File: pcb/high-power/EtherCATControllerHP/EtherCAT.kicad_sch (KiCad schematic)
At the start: 45 parts, among them U7 LAN9252I/ML, U9 24FC512-I/SN, Y2 25 MHz, 20ppm

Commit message: starting HP version
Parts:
- removed C11, C33, C35, C62: 0.1uF, symbol Device:C_Small
- removed C30, C31: 18pF, symbol Device:C_Small
- removed C32, C34: 1uF, symbol Device:C_Small
- removed C71, C72: 10pF, symbol Device:C_Small
- removed R10, R19, R34: 49.9, symbol Device:R_Small
- removed R22: 0, symbol Device:R_Small
- removed R25: 4.7k, symbol Device:R_Small
- removed R26, R43: 2k, symbol Device:R_Small
- removed R7: 12.1K, symbol Device:R_Small
- removed U7: LAN9252I/ML, QFN64_ML_MCH, symbol 2024-07-01_21-03-15:LAN9252I_ML
- removed U9: 24FC512-I/SN, SOIC8_4P9X3P9MC_MCH, symbol 2024-07-03_18-39-37:24FC512-I_SN
- added C38, C39: 18pF, Capacitor_SMD:C_0402_1005Metric, symbol Device:C_Small
- added C50, C53, C55, C57, C75: 0.1uF, Capacitor_SMD:C_0603_1608Metric, symbol Device:C_Small
- added C51, C52: 1uF, Capacitor_SMD:C_0603_1608Metric, symbol Device:C_Small
- added C54: 470pF, Capacitor_SMD:C_0402_1005Metric, symbol Device:C_Small
- added RN1, RN2: 49R9, Resistor_SMD:R_Array_Convex_4x0402, symbol Device:R_Pack04_Split
- added U4: LAN9252I/ML, footprints:QFN64_ML_MCH, symbol 2024-07-01_21-03-15:LAN9252I_ML
- added U7: 24FC512-I/SN, Package_SO:SOP-8_3.9x4.9mm_P1.27mm, symbol 2024-07-03_18-39-37:24FC512-I_SN
- C36: value 0.1uF -> 1uF; footprint (none) -> Capacitor_SMD:C_0603_1608Metric; LCSC Part # (none) -> C106858
- C58: value 1uF -> 0.1uF; footprint (none) -> Capacitor_SMD:C_0603_1608Metric; LCSC Part # (none) -> C77055
- C59, C61, C63: value 0.1uF -> 10pF; footprint (none) -> Capacitor_SMD:C_0402_1005Metric; LCSC Part # (none) -> C115606
- C60: value 470pF -> 10pF; footprint (none) -> Capacitor_SMD:C_0402_1005Metric; LCSC Part # (none) -> C115606
- C64, C65, C66, C67: footprint (none) -> Capacitor_SMD:C_0402_1005Metric; LCSC Part # (none) -> C115606
- C68: footprint (none) -> Capacitor_SMD:C_0402_1005Metric; LCSC Part # (none) -> C147616
- C69: value 10pF -> 0.022uF; footprint (none) -> Capacitor_SMD:C_0402_1005Metric; LCSC Part # (none) -> C147616
- C70: value 10pF -> 0.1uF; footprint (none) -> Capacitor_SMD:C_0603_1608Metric; LCSC Part # (none) -> C77055
- C73: value 0.022uF -> 0.1uF; footprint (none) -> Capacitor_SMD:C_0603_1608Metric; LCSC Part # (none) -> C77055
- FB1, FB2, FB3, FB4: footprint (none) -> Inductor_SMD:L_1206_3216Metric; LCSC Part # (none) -> C380287
- R33, R9: value 49.9 -> 0; footprint (none) -> Resistor_SMD:R_0402_1005Metric; LCSC Part # (none) -> C106231
- R35: value 49.9 -> 4.7k; footprint (none) -> Resistor_SMD:R_0402_1005Metric; LCSC Part # (none) -> C105871
- R36: value 49.9 -> 12.1K; footprint (none) -> Resistor_SMD:R_0402_1005Metric; LCSC Part # (none) -> C281773
- R37: value 0 -> 2k; footprint (none) -> Resistor_SMD:R_0402_1005Metric; LCSC Part # (none) -> C144035
- R8: value 49.9 -> 2k; footprint (none) -> Resistor_SMD:R_0402_1005Metric; LCSC Part # (none) -> C144035
- Y2: value 25 MHz, 20ppm -> ABM8-25.000MHZ-D2Y-T; footprint (none) -> Crystal:Crystal_SMD_3225-4Pin_3.2x2.5mm; LCSC Part # (none) -> C179643; LCSC Part Number C179643 -> (none)
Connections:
- net ETH0_CT1: now also R33.2
- net ETH0_RXN: now also C61.1, RN1.2 (R2.1), U4.61 (RXNB); no longer C65.1, R9.2
- net ETH0_RXP: now also C59.1, RN1.1 (R1.1), U4.60 (RXPB); no longer C64.1, R8.2
- net ETH0_TXN: now also C66.1, RN1.4 (R4.1), U4.63 (TXNB); no longer C67.1
- net ETH0_TXP: now also C64.1, RN1.3 (R3.1), U4.62 (TXPB); no longer C66.1
- net ETH1_CT1: now also C69.1, R9.2; no longer C73.1, R37.2
- net ETH1_RXN: now also C65.1, RN2.3 (R3.1), U4.54 (RXNA); no longer R35.2
- net ETH1_RXP: now also C67.1, RN2.4 (R4.1), U4.55 (RXPA); no longer R36.2
- net ETH1_TXN: now also C60.1, RN2.1 (R1.1), U4.52 (TXNA); no longer C69.1, R33.2
- net ETH1_TXP: now also C63.1, RN2.2 (R2.1), U4.53 (TXPA); no longer C70.1
- net EtherCAT3v3: now also R37.1, R8.1, C75.1, U4.14 (VDDIO), U4.20 (VDDIO), U4.32 (VDDIO), U4.37 (VDDIO), U4.47 (VDDIO), U4.5 (VDD33), U4.7 (REG_EN), U7.8 (VCC)
- net GND: now also R35.2, R36.2, C38.1, C39.1, C50.2, C51.2, C52.2, C53.2, C54.2, C55.2, C57.2, C75.2, U4.10 (FXSDB/FXLOSB/FXSDENB), U4.4 (OSCVSS), U4.41 (TESTMODE), U4.65 (VSS), U4.8 (FXLOSEN), U4.9 (FXSDA/FXLOSA/FXSDENA), U7.4 (VSS)
- net I2C_SCL: now also R37.2, U4.43 (EESCL/TCK), U7.6 (SCL)
- net IRQ: now also U4.44 (IRQ)
- net RST: now also U4.11 (RST#)
- net SPI_CS: now also U4.50 (D5/AD5/OUTVALID/SCS#)
- net SPI_MISO: now also U4.13 (D1/AD1/EOF/SO/SIO1)
- net SPI_MOSI: now also U4.17 (D0/AD0/WD_STATE/SI/SIO0)
- net SPI_SCK: now also U4.19 (D9/AD9/LATCH_IN/SCK)
- net VDDBIAS: now also C53.1, U4.58 (VDD33BIAS); no longer C36.1
- net VDDCR: now also C36.1, C50.1, C54.1, U4.24 (VDDCR), U4.38 (VDDCR), U4.6 (VDDCR); no longer C59.1, C60.1, C61.1
- net VDDTXRX1: now also R33.1, C51.1, C55.1, RN1.5 (R4.2), RN1.6 (R3.2), RN1.7 (R2.2), RN1.8 (R1.2), U4.51 (VDD33TXRX1); no longer R8.1, R9.1
- net VDDTXRX2: now also R9.1, C52.1, C57.1, RN2.5 (R4.2), RN2.6 (R3.2), RN2.7 (R2.2), RN2.8 (R1.2), U4.64 (VDD33TXRX2); no longer R33.1, R35.1, R36.1, R37.1
- net WP: now also R35.1, U7.1 (A0), U7.2 (A1), U7.3 (A2), U7.7 (WP)
- net at Y2.1: now also C38.2, U4.1 (OSCI)
- net at Y2.3: now also C39.2, U4.2 (OSCO)
- net at FB4.1: now also C70.1, C73.1, U4.56 (VDD12TX1), U4.59 (VDD12TX2); no longer C63.1
- new net: R36.1, U4.57 (RBIAS)
- new net I2C_SDA: R8.2, U4.42 (EESDA/TMS), U7.5 (SDA)

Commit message: stash before via stitching
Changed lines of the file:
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@@
 	(wire
 		(pts
-			(xy 314.96 59.69) (xy 312.42 59.69)
-		)
-		(stroke
-			(width 0)
-			(type default)
-		)
-	)
-	(wire
-		(pts
 			(xy 165.1 172.72) (xy 165.1 179.07)
 		)
@@
 	(wire
 		(pts
+			(xy 312.42 59.69) (xy 314.96 59.69)
+		)
+		(stroke
+			(width 0)
+			(type default)
+		)
+	)
+	(wire
+		(pts
 			(xy 92.71 72.39) (xy 92.71 67.31)
 		)
@@
 		)
 	)
-	(hierarchical_label "ETH1_RXP"
+	(hierarchical_label "ETH0_TXP"
 		(shape bidirectional)
-		(at 312.42 82.55 0)
+		(at 312.42 64.77 0)
 		(fields_autoplaced yes)
 		(effects
@@
 		)
 	)
-	(hierarchical_label "ETH0_TXP"
+	(hierarchical_label "ETH0_RXP"
 		(shape bidirectional)
-		(at 312.42 64.77 0)
+		(at 312.42 69.85 0)
 		(fields_autoplaced yes)
 		(effects
@@
 		)
 	)
-	(hierarchical_label "ETH1_TXN"
+	(hierarchical_label "SPI_MISO"
 		(shape bidirectional)
-		(at 312.42 90.17 0)
+		(at 99.06 87.63 180)
+		(fields_autoplaced yes)
+		(effects
+			(font
+				(size 1.27 1.27)
+			)
+			(justify right)
+		)
+	)
+	(hierarchical_label "ETH0_TXN"
+		(shape bidirectional)
+		(at 312.42 62.23 0)
 		(fields_autoplaced yes)
 		(effects
@@
 		)
 	)
-	(hierarchical_label "SPI_MISO"
+	(hierarchical_label "ETH1_RXP"
 		(shape bidirectional)
-		(at 99.06 87.63 180)
+		(at 312.42 82.55 0)
 		(fields_autoplaced yes)
 		(effects
@@
 				(size 1.27 1.27)
 			)
-			(justify right)
+			(justify left)
 		)
 	)
-	(hierarchical_label "ETH0_CT1"
+	(hierarchical_label "ETH1_TXN"
 		(shape bidirectional)
-		(at 209.55 177.8 0)
+		(at 312.42 90.17 0)
 		(fields_autoplaced yes)
 		(effects
@@
 		)
 	)
-	(hierarchical_label "ETH1_RXN"
+	(hierarchical_label "ETH1_TXP"
 		(shape bidirectional)
-		(at 209.55 217.17 0)
+		(at 312.42 87.63 0)
 		(fields_autoplaced yes)
 		(effects
@@
 		)
 	)
-	(hierarchical_label "IRQ"
-		(shape input)
-		(at 314.96 109.22 0)
+	(hierarchical_label "ETH0_CT1"
+		(shape bidirectional)
+		(at 209.55 177.8 0)
 		(fields_autoplaced yes)
 		(effects
@@
 		)
 	)
-	(hierarchical_label "ETH0_TXN"
+	(hierarchical_label "ETH1_RXN"
 		(shape bidirectional)
-		(at 312.42 62.23 0)
+		(at 209.55 217.17 0)
+		(fields_autoplaced yes)
+		(effects
+			(font
+				(size 1.27 1.27)
+			)
+			(justify left)
+		)
+	)
+	(hierarchical_label "IRQ"
+		(shape input)
+		(at 314.96 109.22 0)
 		(fields_autoplaced yes)
 		(effects
@@
 		)
 	)
-	(hierarchical_label "ETH1_TXP"
-		(shape bidirectional)
-		(at 312.42 87.63 0)
-		(fields_autoplaced yes)
-		(effects
-			(font
-				(size 1.27 1.27)
-			)
-			(justify left)
-		)
-	)
-	(hierarchical_label "ETH0_RXP"
-		(shape bidirectional)
-		(at 312.42 69.85 0)
-		(fields_autoplaced yes)
-		(effects
-			(font
-				(size 1.27 1.27)
-			)
-			(justify left)
-		)
-	)
 	(hierarchical_label "SPI_SCK"
 		(shape input)
@@
 		(lib_id "Device:R_Small")
 		(at 189.23 208.28 0)
+		(mirror y)
 		(unit 1)
 		(exclude_from_sim no)
@@
 		(on_board yes)
 		(dnp no)
-		(fields_autoplaced yes)
 		(property "Reference" "R9"
-			(at 191.77 207.0099 0)
+			(at 186.69 207.0099 0)
 			(effects
 				(font
@@
 		)
 		(property "Value" "0"
-			(at 191.77 209.5499 0)
+			(at 186.69 209.5499 0)
 			(effects
 				(font

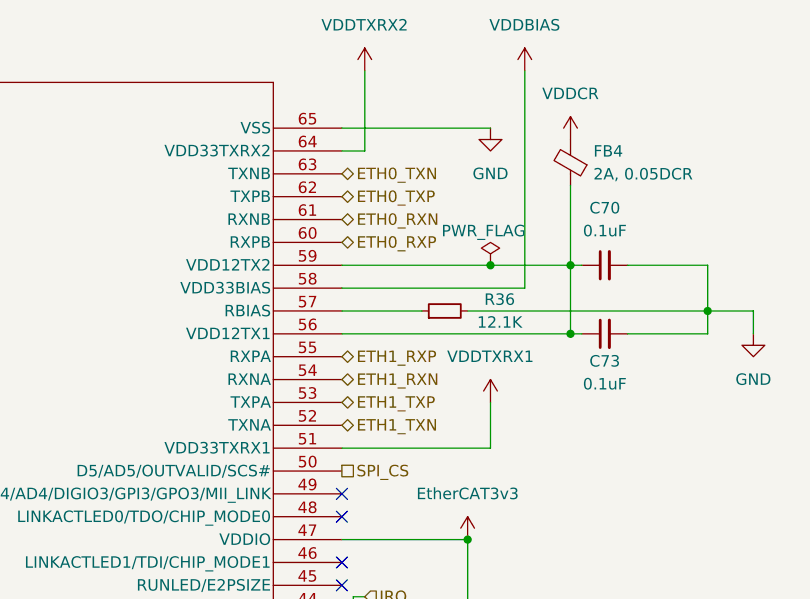
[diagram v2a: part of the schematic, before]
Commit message: redid layout and mounting
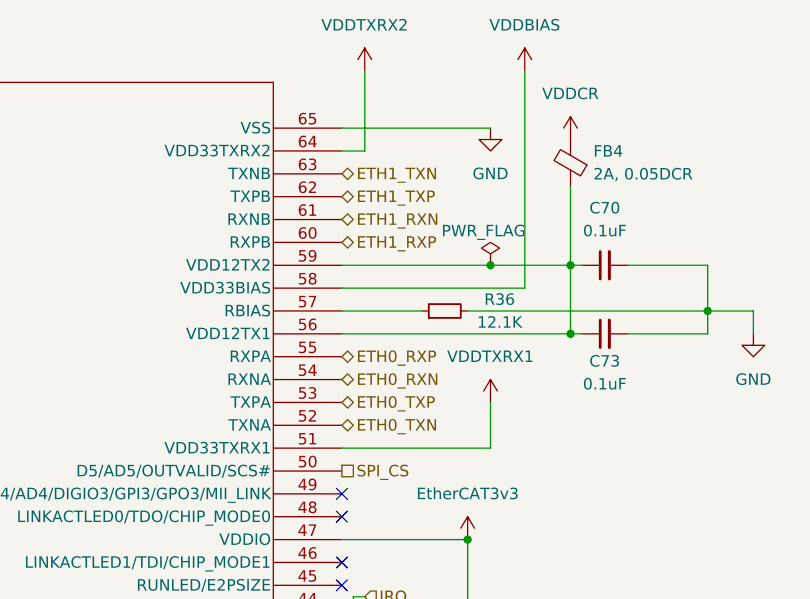
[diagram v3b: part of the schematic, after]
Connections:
- net ETH0_RXN: now also U4.54 (RXNA); no longer U4.61 (RXNB)
- net ETH0_RXP: now also U4.55 (RXPA); no longer U4.60 (RXPB)
- net ETH0_TXN: now also U4.52 (TXNA); no longer U4.63 (TXNB)
- net ETH0_TXP: now also U4.53 (TXPA); no longer U4.62 (TXPB)
- net ETH1_RXN: now also U4.61 (RXNB); no longer U4.54 (RXNA)
- net ETH1_RXP: now also U4.60 (RXPB); no longer U4.55 (RXPA)
- net ETH1_TXN: now also U4.63 (TXNB); no longer U4.52 (TXNA)
- net ETH1_TXP: now also U4.62 (TXPB); no longer U4.53 (TXPA)
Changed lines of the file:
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@@
+		)
+	)
+	(hierarchical_label "ETH1_RXP"
+		(shape bidirectional)
+		(at 312.42 69.85 0)
+		(fields_autoplaced yes)
+		(effects
+			(font
+				(size 1.27 1.27)
+			)
+			(justify left)
+		)
+	)
+	(hierarchical_label "ETH1_TXN"
+		(shape bidirectional)
+		(at 312.42 62.23 0)
+		(fields_autoplaced yes)
+		(effects
+			(font
+				(size 1.27 1.27)
+			)
+			(justify left)
+		)
+	)
+	(hierarchical_label "ETH0_RXP"
+		(shape bidirectional)
+		(at 312.42 82.55 0)
+		(fields_autoplaced yes)
+		(effects
+			(font
+				(size 1.27 1.27)
+			)
+			(justify left)
+		)
+	)
+	(hierarchical_label "SPI_MOSI"
+		(shape bidirectional)
+		(at 99.06 97.79 180)
+		(fields_autoplaced yes)
+		(effects
+			(font
+				(size 1.27 1.27)
+			)
+			(justify right)
+		)
+	)
+	(hierarchical_label "ETH0_TXN"
+		(shape bidirectional)
+		(at 209.55 175.26 0)
+		(fields_autoplaced yes)
+		(effects
+			(font
+				(size 1.27 1.27)
+			)
+			(justify left)
 		)
 	)
 	(hierarchical_label "ETH0_TXP"
 		(shape bidirectional)
+		(at 209.55 172.72 0)
+		(fields_autoplaced yes)
+		(effects
+			(font
+				(size 1.27 1.27)
+			)
+			(justify left)
+		)
+	)
+	(hierarchical_label "ETH1_RXP"
+		(shape bidirectional)
+		(at 209.55 219.71 0)
+		(fields_autoplaced yes)
+		(effects
+			(font
+				(size 1.27 1.27)
+			)
+			(justify left)
+		)
+	)
+	(hierarchical_label "ETH0_TXP"
+		(shape bidirectional)
+		(at 312.42 87.63 0)
+		(fields_autoplaced yes)
+		(effects
+			(font
+				(size 1.27 1.27)
+			)
+			(justify left)
+		)
+	)
+	(hierarchical_label "ETH0_RXN"
+		(shape bidirectional)
+		(at 312.42 85.09 0)
+		(fields_autoplaced yes)
+		(effects
+			(font
+				(size 1.27 1.27)
+			)
+			(justify left)
+		)
+	)
+	(hierarchical_label "SPI_MISO"
+		(shape bidirectional)
+		(at 99.06 87.63 180)
+		(fields_autoplaced yes)
+		(effects
+			(font
+				(size 1.27 1.27)
+			)
+			(justify right)
+		)
+	)
+	(hierarchical_label "ETH0_CT1"
+		(shape bidirectional)
+		(at 209.55 177.8 0)
+		(fields_autoplaced yes)
+		(effects
+			(font
+				(size 1.27 1.27)
+			)
+			(justify left)
+		)
+	)
+	(hierarchical_label "ETH1_RXN"
+		(shape bidirectional)
+		(at 312.42 67.31 0)
+		(fields_autoplaced yes)
+		(effects
+			(font
+				(size 1.27 1.27)
+			)
+			(justify left)
+		)
+	)
+	(hierarchical_label "ETH1_TXP"
+		(shape bidirectional)
 		(at 312.42 64.77 0)
-		(fields_autoplaced yes)
-		(effects
-			(font
-				(size 1.27 1.27)
-			)
-			(justify left)
-		)
-	)
-	(hierarchical_label "ETH0_RXN"
-		(shape bidirectional)
-		(at 312.42 67.31 0)
-		(fields_autoplaced yes)
-		(effects
-			(font
-				(size 1.27 1.27)
-			)
-			(justify left)
-		)
-	)
-	(hierarchical_label "ETH0_RXP"
-		(shape bidirectional)
-		(at 312.42 69.85 0)
-		(fields_autoplaced yes)
-		(effects
-			(font
-				(size 1.27 1.27)
-			)
-			(justify left)
-		)
-	)
-	(hierarchical_label "SPI_MOSI"
-		(shape bidirectional)
-		(at 99.06 97.79 180)
-		(fields_autoplaced yes)
-		(effects
-			(font
-				(size 1.27 1.27)
-			)
-			(justify right)
-		)
-	)
-	(hierarchical_label "ETH0_TXN"
-		(shape bidirectional)
-		(at 209.55 175.26 0)
-		(fields_autoplaced yes)
-		(effects
-			(font
-				(size 1.27 1.27)
-			)
-			(justify left)
-		)
-	)
-	(hierarchical_label "ETH0_TXP"
-		(shape bidirectional)
-		(at 209.55 172.72 0)
-		(fields_autoplaced yes)
-		(effects
-			(font
-				(size 1.27 1.27)
-			)
-			(justify left)
-		)
-	)
-	(hierarchical_label "ETH1_RXP"
-		(shape bidirectional)
-		(at 209.55 219.71 0)
-		(fields_autoplaced yes)
-		(effects
-			(font
-				(size 1.27 1.27)
-			)
-			(justify left)
-		)
-	)
-	(hierarchical_label "SPI_MISO"
-		(shape bidirectional)
-		(at 99.06 87.63 180)
-		(fields_autoplaced yes)
-		(effects
-			(font
-				(size 1.27 1.27)
-			)
-			(justify right)
-		)
-	)
-	(hierarchical_label "ETH0_TXN"
-		(shape bidirectional)
-		(at 312.42 62.23 0)
-		(fields_autoplaced yes)
-		(effects
-			(font
-				(size 1.27 1.27)
-			)
-			(justify left)
-		)
-	)
-	(hierarchical_label "ETH1_RXP"
-		(shape bidirectional)
-		(at 312.42 82.55 0)
-		(fields_autoplaced yes)
-		(effects
-			(font
-				(size 1.27 1.27)
-			)
-			(justify left)
-		)
-	)
-	(hierarchical_label "ETH1_TXN"
-		(shape bidirectional)
-		(at 312.42 90.17 0)
-		(fields_autoplaced yes)
-		(effects
-			(font
-				(size 1.27 1.27)
-			)
-			(justify left)
-		)
-	)
-	(hierarchical_label "ETH1_RXN"
-		(shape bidirectional)
-		(at 312.42 85.09 0)
-		(fields_autoplaced yes)
-		(effects
-			(font
-				(size 1.27 1.27)
-			)
-			(justify left)
-		)
-	)
-	(hierarchical_label "ETH1_TXP"
-		(shape bidirectional)
-		(at 312.42 87.63 0)
-		(fields_autoplaced yes)
-		(effects
-			(font
-				(size 1.27 1.27)
-			)
-			(justify left)
-		)
-	)
-	(hierarchical_label "ETH0_CT1"
-		(shape bidirectional)
-		(at 209.55 177.8 0)
 		(fields_autoplaced yes)
 		(effects
@@
 		(fields_autoplaced yes)
 		(effects
+			(font
+				(size 1.27 1.27)
+			)
+			(justify left)
+		)
+	)
+	(hierarchical_label "ETH0_TXN"
+		(shape bidirectional)
+		(at 312.42 90.17 0)
+		(fields_autoplaced yes)
+		(effects
